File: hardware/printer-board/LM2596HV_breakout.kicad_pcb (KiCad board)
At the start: 2 copper layers, 50 x 30 mm, 13 parts, among them J1 VIN, J2 VOUT, U1 LM2596HVS

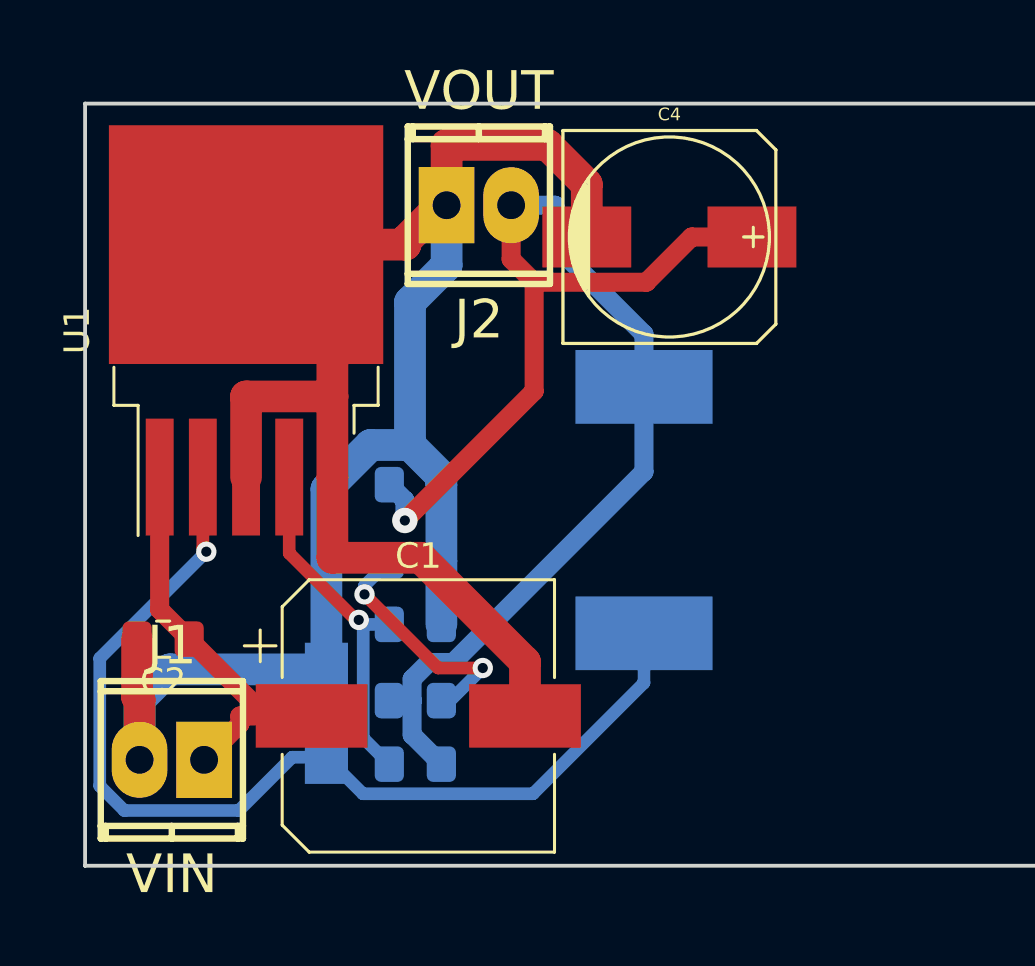
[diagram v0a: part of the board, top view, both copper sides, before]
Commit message: update power circuit,
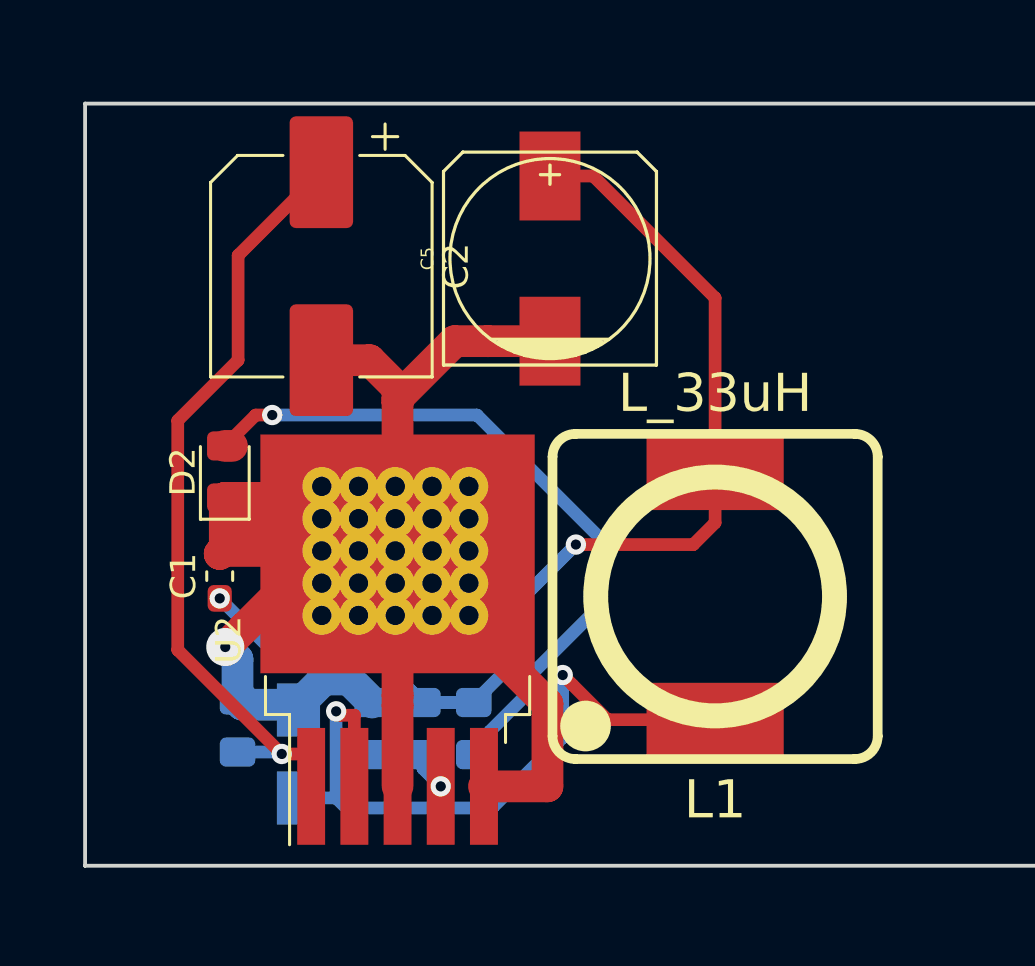
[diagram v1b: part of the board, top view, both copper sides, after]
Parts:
- removed C4: CP220uf,35V, w_smd_cap:c_elec_8x10.5
- removed J1: VIN, footprint-lib:mpt_0,5%2f2-2,54
- removed J2: VOUT, footprint-lib:mpt_0,5%2f2-2,54
- removed U1: LM2596HVS, Package_TO_SOT_SMD:TO-263-5_TabPin3
- added C5: CP220uf,35V, w_smd_cap:c_elec_8x10.5, F.Cu at (33.3, 21.1)
- added U2: LM2596HVS, footprint-lib:TO-263-5_TabPin3,heat_drill, F.Cu at (27.3, 36.1)
- C1: value CP100uf,63V -> C103,0603; footprint Capacitor_SMD:CP_Elec_10x10.5 -> Capacitor_SMD:C_0603_1608Metric_Pad1.05x0.95mm_HandSolder
- C2: value C103 -> CP100uf,50V; footprint Capacitor_SMD:C_0805_2012Metric_Pad1.15x1.40mm_HandSolder -> Capacitor_SMD:CP_Elec_8x10.5
- D2: value LED_GREEN -> 5V_STATUS; moved to F.Cu
- L1: moved to F.Cu
- R1: value RVAR -> R331
- R2: value R331 -> RVAR
- moved C2 15.9 mm to (24.3, 21.4), turned to 270 degrees
- moved C3 11.8 mm to (21.0, 39.5), turned to 90 degrees
- moved C1 9.56 mm to (20.3, 33.6), turned to 90 degrees
- moved D2 8.28 mm to (20.5, 29.5), turned to 90 degrees
- moved L1 4.40 mm to (39.8, 34.4), turned to 180 degrees
- moved R2 4.11 mm to (28.3, 39.6), turned to 270 degrees
- moved R3 2.55 mm to (30.3, 39.6), turned to 270 degrees
- moved R1 2.20 mm to (26.3, 39.6), turned to 270 degrees
- moved D1 1.94 mm to (23.4, 40.6)
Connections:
- C1 pad 1: VIN -> +5V
- C2 pad 1: VIN -> +12V
- C3 pad 1: VOUT -> +12V
- L1 pad 2: VOUT -> +5V
- R1 pad 1: VOUT -> GND
- R2 pad 1: GND -> +5V
- R3 pad 1: VOUT -> +5V
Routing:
- net VOUT: track 56.8 -> 0.00 mm, vias 1 -> 0
- net +5V: track 0.00 -> 42.8 mm, vias 0 -> 2
- net +12V: track 0.00 -> 31.1 mm, vias 0 -> 1
- net Net-(D2-Pad2): track 9.74 -> 28.1 mm, vias 2 -> 1
- net VIN: track 16.3 -> 0.00 mm
- net Net-(D1-Pad1): track 41.0 -> 27.9 mm, vias 1 -> 2
- net Net-(R1-Pad2): track 14.0 -> 3.54 mm
- net GND: track 93.7 -> 87.3 mm, vias 0 -> 1

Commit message: update for stepper Z,
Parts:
- added C10: CP100uf,25V, Capacitor_SMD:CP_Elec_6.3x7.7, F.Cu at (297.3, 53.2)
- added C11: C104,0603, Capacitor_SMD:C_0603_1608Metric_Pad1.05x0.95mm_HandSolder, F.Cu at (297.6, 59.1)
- added C12: CP100uf,25V, Capacitor_SMD:CP_Elec_6.3x7.7, F.Cu at (240.3, 109.1)
- added C13: C104,0603, Capacitor_SMD:C_0603_1608Metric_Pad1.05x0.95mm_HandSolder, F.Cu at (237.3, 115.0)
- added C14: C106,0603, Capacitor_SMD:C_0603_1608Metric_Pad1.05x0.95mm_HandSolder, F.Cu at (295.6, 127.7)
- added C15: C106,0603, Capacitor_SMD:C_0603_1608Metric_Pad1.05x0.95mm_HandSolder, F.Cu at (292.3, 136.8)
- added C16: C106,0603, Capacitor_SMD:C_0603_1608Metric_Pad1.05x0.95mm_HandSolder, F.Cu at (292.3, 127.7)
- added C17: C106,0603, Capacitor_SMD:C_0603_1608Metric_Pad1.05x0.95mm_HandSolder, F.Cu at (295.6, 129.2)
- added C18: C106,0603, Capacitor_SMD:C_0603_1608Metric_Pad1.05x0.95mm_HandSolder, F.Cu at (292.3, 132.3)
- added C19: C104,0603, Capacitor_SMD:C_0603_1608Metric_Pad1.05x0.95mm_HandSolder, F.Cu at (221.4, 140.3)
- added C20: CP100uf,35V, Capacitor_SMD:CP_Elec_6.3x7.7, F.Cu at (235.1, 137.6)
- added C21: C104,0603, Capacitor_SMD:C_0603_1608Metric_Pad1.05x0.95mm_HandSolder, F.Cu at (295.3, 86.0)
- added C22: C10pf,0603, Capacitor_SMD:C_0603_1608Metric_Pad1.05x0.95mm_HandSolder, F.Cu at (281.9, 85.8)
- added C23: C104,0603, Capacitor_SMD:C_0603_1608Metric_Pad1.05x0.95mm_HandSolder, F.Cu at (308.3, 76.8)
- added C24: C10pf,0603, Capacitor_SMD:C_0603_1608Metric_Pad1.05x0.95mm_HandSolder, F.Cu at (285.2, 85.8)
- added C25: C104,0603, Capacitor_SMD:C_0603_1608Metric_Pad1.05x0.95mm_HandSolder, F.Cu at (295.1, 82.0)
- added C26: C104,0603, Capacitor_SMD:C_0603_1608Metric_Pad1.05x0.95mm_HandSolder, F.Cu at (295.1, 80.4)
- added C27: C104,0603, Capacitor_SMD:C_0603_1608Metric_Pad1.05x0.95mm_HandSolder, F.Cu at (298.5, 80.4)
- added C28: C104,0603, Capacitor_SMD:C_0603_1608Metric_Pad1.05x0.95mm_HandSolder, F.Cu at (295.1, 83.5)
- added C29: C105,0603, Capacitor_SMD:C_0603_1608Metric_Pad1.05x0.95mm_HandSolder, F.Cu at (305.0, 75.3)
- added C30: C104,0603, Capacitor_SMD:C_0603_1608Metric_Pad1.05x0.95mm_HandSolder, F.Cu at (298.5, 78.9)
- added C31: C104,0603, Capacitor_SMD:C_0603_1608Metric_Pad1.05x0.95mm_HandSolder, F.Cu at (291.9, 85.8)
- added C32: C104,0603, Capacitor_SMD:C_0603_1608Metric_Pad1.05x0.95mm_HandSolder, F.Cu at (288.6, 85.8)
- added C33: CP220uf,16V, Capacitor_SMD:C_0603_1608Metric_Pad1.05x0.95mm_HandSolder, F.Cu at (147.7, 149.0)
- added C34: CP220uf,16V, Capacitor_SMD:C_0603_1608Metric_Pad1.05x0.95mm_HandSolder, F.Cu at (144.3, 149.0)
- added C35: CP220uf,25V, Capacitor_SMD:C_0603_1608Metric_Pad1.05x0.95mm_HandSolder, F.Cu at (144.3, 150.5)
- added C36: CP100uf,16V, Capacitor_SMD:CP_Elec_6.3x5.3, F.Cu at (259.2, 130.5)
- added C37: CP100uf,16V, Capacitor_SMD:CP_Elec_6.3x5.3, F.Cu at (321.8, 48.1)
- added C38: CP100uf,16V, Capacitor_SMD:CP_Elec_6.3x5.3, F.Cu at (259.2, 145.1)
- added C39: CP100uf,25V, Capacitor_SMD:CP_Elec_6.3x7.7, F.Cu at (257.2, 77.0)
- added C4: CP100uf,25V, Capacitor_SMD:CP_Elec_6.3x7.7, F.Cu at (200.2, 109.1)
- added C40: C104,0603, Capacitor_SMD:C_0603_1608Metric_Pad1.05x0.95mm_HandSolder, F.Cu at (254.2, 84.5)
- added C41: CP100uf,25V, Capacitor_SMD:CP_Elec_6.3x7.7, F.Cu at (257.2, 53.2)
- added C42: C104,0603, Capacitor_SMD:C_0603_1608Metric_Pad1.05x0.95mm_HandSolder, F.Cu at (263.6, 54.0)
- added C43: C104,0603, Capacitor_SMD:C_0603_1608Metric_Pad1.05x0.95mm_HandSolder, F.Cu at (274.0, 103.0)
- added C44: CP100uf,16V, Capacitor_SMD:CP_Elec_6.3x5.3, F.Cu at (280.3, 95.8)
- added C45: C106,0603, Capacitor_SMD:C_0603_1608Metric_Pad1.05x0.95mm_HandSolder, F.Cu at (318.6, 92.3)
- added C46: C104,0603, Capacitor_SMD:C_0603_1608Metric_Pad1.05x0.95mm_HandSolder, F.Cu at (325.3, 92.3)
- added C47: C332,0603, Capacitor_SMD:C_0603_1608Metric_Pad1.05x0.95mm_HandSolder, F.Cu at (322.0, 92.3)
- added C48: C103,0603, Capacitor_SMD:C_0603_1608Metric_Pad1.05x0.95mm_HandSolder, F.Cu at (318.6, 93.8)
- added C49: C226,6.3v,0603, Capacitor_SMD:C_0603_1608Metric_Pad1.05x0.95mm_HandSolder, F.Cu at (328.7, 93.8)
- added C50: C106,0603, Capacitor_SMD:C_0603_1608Metric_Pad1.05x0.95mm_HandSolder, F.Cu at (224.8, 152.9)
- added C51: C104,0603, Capacitor_SMD:C_0603_1608Metric_Pad1.05x0.95mm_HandSolder, F.Cu at (228.1, 151.4)
- added C52: C332,0603, Capacitor_SMD:C_0603_1608Metric_Pad1.05x0.95mm_HandSolder, F.Cu at (221.4, 152.9)
- added C53: C103,0603, Capacitor_SMD:C_0603_1608Metric_Pad1.05x0.95mm_HandSolder, F.Cu at (224.8, 151.4)
- added C54: C226,6.3v,0603, Capacitor_SMD:C_0603_1608Metric_Pad1.05x0.95mm_HandSolder, F.Cu at (221.4, 151.4)
- added C6: CP100uf,25V, Capacitor_SMD:CP_Elec_6.3x7.7, F.Cu at (160.0, 133.1)
- added C7: C104,0603, Capacitor_SMD:C_0603_1608Metric_Pad1.05x0.95mm_HandSolder, F.Cu at (160.3, 139.0)
- added C8: CP100uf,25V, Capacitor_SMD:CP_Elec_6.3x7.7, F.Cu at (200.1, 133.1)
- added C9: C104,0603, Capacitor_SMD:C_0603_1608Metric_Pad1.05x0.95mm_HandSolder, F.Cu at (197.1, 140.5)
- added D10: LED_BLUE,0603, LED_SMD:LED_0603_1608Metric_Pad1.05x0.95mm_HandSolder, F.Cu at (315.2, 79.3)
- added D11: LED_BLUE,0603, LED_SMD:LED_0603_1608Metric_Pad1.05x0.95mm_HandSolder, F.Cu at (318.6, 79.3)
- added D12: LED_BLUE,0603, LED_SMD:LED_0603_1608Metric_Pad1.05x0.95mm_HandSolder, F.Cu at (318.6, 80.9)
- added D13: LED_BLUE,0603, LED_SMD:LED_0603_1608Metric_Pad1.05x0.95mm_HandSolder, F.Cu at (325.4, 79.3)
- added D14: LED_BLUE,0603, LED_SMD:LED_0603_1608Metric_Pad1.05x0.95mm_HandSolder, F.Cu at (322.0, 79.3)
- added D15: SD_M4, Diode_SMD:D_SOD-323_HandSoldering, F.Cu at (221.8, 136.1)
- added D16: SD_M4, Diode_SMD:D_SOD-323_HandSoldering, F.Cu at (225.8, 136.1)
- added D17: PB9, LED_SMD:LED_0603_1608Metric_Pad1.05x0.95mm_HandSolder, F.Cu at (278.5, 85.8)
- added D18: LED_RED,0603, LED_SMD:LED_0603_1608Metric_Pad1.05x0.95mm_HandSolder, F.Cu at (295.3, 102.5)
- added D19: LED_RED,0603, LED_SMD:LED_0603_1608Metric_Pad1.05x0.95mm_HandSolder, F.Cu at (265.4, 122.5)
- added D20: LED_BLUE,0603, LED_SMD:LED_0603_1608Metric_Pad1.05x0.95mm_HandSolder, F.Cu at (259.8, 134.9)
- added D21: LED_BLUE,0603, LED_SMD:LED_0603_1608Metric_Pad1.05x0.95mm_HandSolder, F.Cu at (322.4, 52.4)
- added D22: LED_BLUE,0603, LED_SMD:LED_0603_1608Metric_Pad1.05x0.95mm_HandSolder, F.Cu at (272.1, 142.3)
- added D23: LED_BLUE,0603, LED_SMD:LED_0603_1608Metric_Pad1.05x0.95mm_HandSolder, F.Cu at (254.2, 81.4)
- added D24: LED_BLUE,0603, LED_SMD:LED_0603_1608Metric_Pad1.05x0.95mm_HandSolder, F.Cu at (254.2, 57.5)
- added D3: LED_BLUE,0603, LED_SMD:LED_0603_1608Metric_Pad1.05x0.95mm_HandSolder, F.Cu at (197.2, 113.5)
- added D4: LED_BLUE,0603, LED_SMD:LED_0603_1608Metric_Pad1.05x0.95mm_HandSolder, F.Cu at (157.0, 137.4)
- added D5: LED_BLUE,0603, LED_SMD:LED_0603_1608Metric_Pad1.05x0.95mm_HandSolder, F.Cu at (197.1, 137.4)
- added D6: LED_BLUE,0603, LED_SMD:LED_0603_1608Metric_Pad1.05x0.95mm_HandSolder, F.Cu at (294.3, 57.5)
- added D7: LED_BLUE,0603, LED_SMD:LED_0603_1608Metric_Pad1.05x0.95mm_HandSolder, F.Cu at (237.3, 113.5)
- added D8: LED_RED,0603, LED_SMD:LED_0603_1608Metric_Pad1.05x0.95mm_HandSolder, F.Cu at (295.3, 119.1)
- added D9: LED_BLUE,0603, LED_SMD:LED_0603_1608Metric_Pad1.05x0.95mm_HandSolder, F.Cu at (315.2, 80.9)
- added F1: 16V/30A, w_misc_comp:fuse_smf, F.Cu at (225.0, 127.0)
- added F2: 30V/5A, w_misc_comp:fuse_smf, F.Cu at (225.0, 132.4)
- added H1: MOUNT_M3, MountingHole:MountingHole_2.7mm_M2.5, F.Cu at (3.00, 3.00)
- added H2: MOUNT_M3, MountingHole:MountingHole_2.7mm_M2.5, F.Cu at (97.0, 3.00)
- added H3: MOUNT_M3, MountingHole:MountingHole_2.7mm_M2.5, F.Cu at (3.00, 97.0)
- added H4: MOUNT_M3, MountingHole:MountingHole_2.7mm_M2.5, F.Cu at (97.0, 97.0)
- added J1: USB_DEBUG, Connector_PinHeader_1.27mm:PinHeader_1x05_P1.27mm_Vertical, F.Cu at (187.4, 45.7)
- added J10: MS_SELECT, Connector_PinHeader_2.54mm:PinHeader_2x03_P2.54mm_Vertical, F.Cu at (304.8, 46.3)
- added J11: E0, footprint-lib:b4b-ph-kl,stepper_terminal, F.Cu at (297.8, 46.6)
- added J12: MS_SELECT, Connector_PinHeader_2.54mm:PinHeader_2x03_P2.54mm_Vertical, F.Cu at (247.8, 102.3)
- added J13: E1, footprint-lib:b4b-ph-kl,stepper_terminal, F.Cu at (240.8, 102.6)
- added J14: HEATBED, footprint-lib:mpt_0,5%2f2-2,54,heatbed, F.Cu at (309.5, 113.4)
- added J15: X_MIN, footprint-lib:b3b-ph-kl,end_stop, F.Cu at (317.7, 70.5)
- added J16: X_MAX, footprint-lib:b3b-ph-kl,end_stop, F.Cu at (317.7, 75.6)
- added J17: Y_MIN, footprint-lib:b3b-ph-kl,end_stop, F.Cu at (326.1, 70.5)
- added J18: Y_MAX, footprint-lib:b3b-ph-kl,end_stop, F.Cu at (326.1, 75.6)
- added J19: Z_MIN, footprint-lib:b3b-ph-kl,end_stop, F.Cu at (334.5, 70.5)
- added J2: MS_SELECT, Connector_PinHeader_2.54mm:PinHeader_2x03_P2.54mm_Vertical, F.Cu at (167.5, 102.3)
- added J20: Z_MAX, footprint-lib:b3b-ph-kl,end_stop, F.Cu at (334.5, 75.6)
- added J21: HEATBED_TEMP, w_conn_jst-ph:b2b-ph-kl, F.Cu at (281.1, 134.1)
- added J22: HOTEND_TEMP0, w_conn_jst-ph:b2b-ph-kl, F.Cu at (281.1, 129.1)
- added J23: HOTEND_TEMP1, w_conn_jst-ph:b2b-ph-kl, F.Cu at (287.4, 129.1)
- added J24: AUX_TEMP, w_conn_jst-ph:b2b-ph-kl, F.Cu at (287.4, 134.1)
- added J25: 12V_INPUT_2, footprint-lib:mpt_0,5%2f2-2,54,12V_SRC, F.Cu at (245.3, 130.8)
- added J26: 12V_INPUT, footprint-lib:mpt_0,5%2f2-2,54,12V_SRC, F.Cu at (239.3, 130.8)
- added J27: 12V_OUT, footprint-lib:mpt_0,5%2f2-2,54,12V_SRC, F.Cu at (233.3, 130.8)
- added J28: SWD, Connector_PinHeader_1.27mm:PinHeader_1x04_P1.27mm_Vertical, F.Cu at (307.2, 69.6)
- added J29: USB_DEBUG, Connector_PinHeader_1.27mm:PinHeader_1x05_P1.27mm_Vertical, F.Cu at (157.4, 149.5)
- added J3: X, footprint-lib:b4b-ph-kl,stepper_terminal, F.Cu at (160.5, 102.6)
- added J30: PWR_DEBUG, Connector_PinHeader_1.27mm:PinHeader_1x05_P1.27mm_Vertical, F.Cu at (141.1, 149.5)
- added J31: HOT_END, footprint-lib:mpt_0,5%2f2-2,54,heatbed, F.Cu at (309.5, 96.8)
- added J32: HOT_END, footprint-lib:mpt_0,5%2f2-2,54,heatbed, F.Cu at (279.6, 116.8)
- added J33: TO FAN0, footprint-lib:b2b-ph-kl,fan_pwm_out, F.Cu at (267.2, 129.1)
- added J34: TO FAN1, footprint-lib:b2b-ph-kl,fan_pwm_out, F.Cu at (329.8, 46.6)
- added J35: TO FAN2, footprint-lib:b2b-ph-kl,fan_pwm_out, F.Cu at (267.2, 143.6)
- added J36: MS_SELECT, Connector_PinHeader_2.54mm:PinHeader_2x03_P2.54mm_Vertical, F.Cu at (264.7, 70.2)
- added J37: Z2, footprint-lib:b4b-ph-kl,stepper_terminal, F.Cu at (257.7, 70.5)
- added J38: MS_SELECT, Connector_PinHeader_2.54mm:PinHeader_2x03_P2.54mm_Vertical, F.Cu at (264.7, 46.3)
- added J39: Y, footprint-lib:b4b-ph-kl,stepper_terminal, F.Cu at (257.7, 46.6)
- added J4: MS_SELECT, Connector_PinHeader_2.54mm:PinHeader_2x03_P2.54mm_Vertical, F.Cu at (207.7, 102.3)
- added J40: Conn_01x07, Connector_PinHeader_1.27mm:PinHeader_1x07_P1.27mm_Vertical, F.Cu at (273.9, 93.4)
- added J41: EXP1, Connector_PinHeader_2.54mm:PinHeader_2x05_P2.54mm_Vertical, F.Cu at (261.8, 94.1)
- added J42: EXP2, Connector_PinHeader_2.54mm:PinHeader_2x05_P2.54mm_Vertical, F.Cu at (268.0, 94.1)
- added J5: Z, footprint-lib:b4b-ph-kl,stepper_terminal, F.Cu at (200.7, 102.6)
- added J6: MS_SELECT, Connector_PinHeader_2.54mm:PinHeader_2x03_P2.54mm_Vertical, F.Cu at (167.5, 126.2)
- added J7: Z1, footprint-lib:b4b-ph-kl,stepper_terminal, F.Cu at (160.5, 126.5)
- added J8: MS_SELECT, Connector_PinHeader_2.54mm:PinHeader_2x03_P2.54mm_Vertical, F.Cu at (207.6, 126.2)
- added J9: Z3, footprint-lib:b4b-ph-kl,stepper_terminal, F.Cu at (200.6, 126.5)
- added JP1: Jumper_NO_Small, Jumper:SolderJumper-2_P1.3mm_Open_TrianglePad1.0x1.5mm, F.Cu at (141.2, 95.7)
- added JP2: Jumper_NO_Small, Jumper:SolderJumper-2_P1.3mm_Open_TrianglePad1.0x1.5mm, F.Cu at (187.5, 54.7)
- added JP3: Jumper_NO_Small, Jumper:SolderJumper-2_P1.3mm_Open_TrianglePad1.0x1.5mm, F.Cu at (194.0, 45.8)
- added JP4: Jumper_NO_Small, Jumper:SolderJumper-2_P1.3mm_Open_TrianglePad1.0x1.5mm, F.Cu at (144.6, 94.1)
- added JP5: Jumper_NO_Small, SolderJumper-2_P1.3mm_Open_TrianglePad1.0x1.5mm, F.Cu at (221.4, 138.3)
- added JP6: Jumper_NO_Small, SolderJumper-2_P1.3mm_Open_TrianglePad1.0x1.5mm, F.Cu at (298.5, 84.0)
- added JP7: Jumper_NO_Small, SolderJumper-2_P1.3mm_Open_TrianglePad1.0x1.5mm, F.Cu at (305.2, 78.8)
- added L2: L_15uH, w_smd_inductors:inductor_smd_4.8x2.8mm, F.Cu at (327.2, 88.8)
- added L3: L_15uH, w_smd_inductors:inductor_smd_4.8x2.8mm, F.Cu at (229.9, 147.9)
- added Q1: WSK220N04, footprint-lib:TO-263-2,drill_array, F.Cu at (298.1, 112.6)
- added Q2: STP55NF06, footprint-lib:TO-263-2,drill_array, F.Cu at (298.1, 96.0)
- added Q3: STP55NF06, footprint-lib:TO-263-2,drill_array, F.Cu at (268.3, 116.0)
- added Q4: D882, footprint-lib:SOT-89-3,thermal_vias, F.Cu at (266.5, 134.6)
- added Q5: D882, footprint-lib:SOT-89-3,thermal_vias, F.Cu at (329.1, 52.2)
- added Q6: D882, footprint-lib:SOT-89-3,thermal_vias, F.Cu at (266.5, 149.2)
- added R10: R103,0603, Resistor_SMD:R_0603_1608Metric_Pad1.05x0.95mm_HandSolder, F.Cu at (160.4, 115.4)
- added R11: R104,0603, Resistor_SMD:R_0603_1608Metric_Pad1.05x0.95mm_HandSolder, F.Cu at (197.2, 115.0)
- added R12: R102,0603, Resistor_SMD:R_0603_1608Metric_Pad1.05x0.95mm_HandSolder, F.Cu at (206.6, 109.9)
- added R13: R103,0603, Resistor_SMD:R_0603_1608Metric_Pad1.05x0.95mm_HandSolder, F.Cu at (200.5, 115.0)
- added R14: R104,0603, Resistor_SMD:R_0603_1608Metric_Pad1.05x0.95mm_HandSolder, F.Cu at (166.4, 133.9)
- added R15: R102,0603, Resistor_SMD:R_0603_1608Metric_Pad1.05x0.95mm_HandSolder, F.Cu at (157.0, 139.0)
- added R16: R103,0603, Resistor_SMD:R_0603_1608Metric_Pad1.05x0.95mm_HandSolder, F.Cu at (157.0, 140.5)
- added R17: R104,0603, Resistor_SMD:R_0603_1608Metric_Pad1.05x0.95mm_HandSolder, F.Cu at (197.1, 139.0)
- added R18: R102,0603, Resistor_SMD:R_0603_1608Metric_Pad1.05x0.95mm_HandSolder, F.Cu at (206.5, 133.9)
- added R19: R103,0603, Resistor_SMD:R_0603_1608Metric_Pad1.05x0.95mm_HandSolder, F.Cu at (200.4, 139.0)
- added R20: R104,0603, Resistor_SMD:R_0603_1608Metric_Pad1.05x0.95mm_HandSolder, F.Cu at (303.7, 54.0)
- added R21: R102,0603, Resistor_SMD:R_0603_1608Metric_Pad1.05x0.95mm_HandSolder, F.Cu at (294.3, 60.6)
- added R22: R103,0603, Resistor_SMD:R_0603_1608Metric_Pad1.05x0.95mm_HandSolder, F.Cu at (294.3, 59.1)
- added R23: R104,0603, Resistor_SMD:R_0603_1608Metric_Pad1.05x0.95mm_HandSolder, F.Cu at (240.6, 115.0)
- added R24: R102,0603, Resistor_SMD:R_0603_1608Metric_Pad1.05x0.95mm_HandSolder, F.Cu at (246.7, 109.9)
- added R25: R103,0603, Resistor_SMD:R_0603_1608Metric_Pad1.05x0.95mm_HandSolder, F.Cu at (237.3, 116.6)
- added R26: R100,0805, Resistor_SMD:R_0805_2012Metric_Pad1.15x1.40mm_HandSolder, F.Cu at (308.3, 117.6)
- added R27: R104,0805, Resistor_SMD:R_0805_2012Metric_Pad1.15x1.40mm_HandSolder, F.Cu at (291.7, 119.3)
- added R28: R182,0603, Resistor_SMD:R_0603_1608Metric_Pad1.05x0.95mm_HandSolder, F.Cu at (298.6, 119.0)
- added R29: R102,0603, Resistor_SMD:R_0603_1608Metric_Pad1.05x0.95mm_HandSolder, F.Cu at (332.0, 82.3)
- added R30: R102,0603, Resistor_SMD:R_0603_1608Metric_Pad1.05x0.95mm_HandSolder, F.Cu at (328.7, 79.3)
- added R31: R102,0603, Resistor_SMD:R_0603_1608Metric_Pad1.05x0.95mm_HandSolder, F.Cu at (325.3, 80.9)
- added R32: R102,0603, Resistor_SMD:R_0603_1608Metric_Pad1.05x0.95mm_HandSolder, F.Cu at (328.7, 80.8)
- added R33: R102,0603, Resistor_SMD:R_0603_1608Metric_Pad1.05x0.95mm_HandSolder, F.Cu at (328.7, 82.3)
- added R34: R102,0603, Resistor_SMD:R_0603_1608Metric_Pad1.05x0.95mm_HandSolder, F.Cu at (322.0, 80.9)
- added R35: R472,0603, Resistor_SMD:R_0603_1608Metric_Pad1.05x0.95mm_HandSolder, F.Cu at (292.3, 129.2)
- added R36: R472,0603, Resistor_SMD:R_0603_1608Metric_Pad1.05x0.95mm_HandSolder, F.Cu at (292.3, 130.7)
- added R37: R472,0603, Resistor_SMD:R_0603_1608Metric_Pad1.05x0.95mm_HandSolder, F.Cu at (292.3, 135.3)
- added R38: R472,0603, Resistor_SMD:R_0603_1608Metric_Pad1.05x0.95mm_HandSolder, F.Cu at (295.6, 132.3)
- added R39: R472,0603, Resistor_SMD:R_0603_1608Metric_Pad1.05x0.95mm_HandSolder, F.Cu at (292.3, 133.8)
- added R4: R220,0603, Resistor_SMD:R_0603_1608Metric_Pad1.05x0.95mm_HandSolder, F.Cu at (187.5, 52.7)
- added R40: R472,0603, Resistor_SMD:R_0603_1608Metric_Pad1.05x0.95mm_HandSolder, F.Cu at (301.8, 82.0)
- added R41: R472,0603, Resistor_SMD:R_0603_1608Metric_Pad1.05x0.95mm_HandSolder, F.Cu at (301.8, 80.4)
- added R42: R0,0603, Resistor_SMD:R_0603_1608Metric_Pad1.05x0.95mm_HandSolder, F.Cu at (308.3, 75.3)
- added R43: R0,0603, Resistor_SMD:R_0603_1608Metric_Pad1.05x0.95mm_HandSolder, F.Cu at (295.1, 78.9)
- added R44: R102,0603, Resistor_SMD:R_0603_1608Metric_Pad1.05x0.95mm_HandSolder, F.Cu at (301.8, 78.9)
- added R45: R103,0603, Resistor_SMD:R_0603_1608Metric_Pad1.05x0.95mm_HandSolder, F.Cu at (305.0, 76.8)
- added R46: R103,0603, Resistor_SMD:R_0603_1608Metric_Pad1.05x0.95mm_HandSolder, F.Cu at (298.5, 82.0)
- added R47: R220,0603, Resistor_SMD:R_0603_1608Metric_Pad1.05x0.95mm_HandSolder, F.Cu at (160.7, 150.5)
- added R48: R220,0603, Resistor_SMD:R_0603_1608Metric_Pad1.05x0.95mm_HandSolder, F.Cu at (164.0, 149.0)
- added R49: R152,0603, Resistor_SMD:R_0603_1608Metric_Pad1.05x0.95mm_HandSolder, F.Cu at (160.7, 149.0)
- added R5: R220,0603, Resistor_SMD:R_0603_1608Metric_Pad1.05x0.95mm_HandSolder, F.Cu at (147.9, 93.6)
- added R50: R100,0805, Resistor_SMD:R_0805_2012Metric_Pad1.15x1.40mm_HandSolder, F.Cu at (308.3, 101.0)
- added R51: R104,0805, Resistor_SMD:R_0805_2012Metric_Pad1.15x1.40mm_HandSolder, F.Cu at (291.7, 102.7)
- added R52: R182,0603, Resistor_SMD:R_0603_1608Metric_Pad1.05x0.95mm_HandSolder, F.Cu at (298.6, 102.4)
- added R53: R100,0805, Resistor_SMD:R_0805_2012Metric_Pad1.15x1.40mm_HandSolder, F.Cu at (261.8, 122.7)
- added R54: R104,0805, Resistor_SMD:R_0805_2012Metric_Pad1.15x1.40mm_HandSolder, F.Cu at (278.5, 121.0)
- added R55: R182,0603, Resistor_SMD:R_0603_1608Metric_Pad1.05x0.95mm_HandSolder, F.Cu at (268.8, 122.5)
- added R56: R100,0805, Resistor_SMD:R_0805_2012Metric_Pad1.15x1.40mm_HandSolder, F.Cu at (272.3, 127.9)
- added R57: R104,0805, Resistor_SMD:R_0805_2012Metric_Pad1.15x1.40mm_HandSolder, F.Cu at (256.2, 135.1)
- added R58: R100,0603, Resistor_SMD:R_0603_1608Metric_Pad1.05x0.95mm_HandSolder, F.Cu at (259.4, 136.8)
- added R59: R182,0603, Resistor_SMD:R_0603_1608Metric_Pad1.05x0.95mm_HandSolder, F.Cu at (256.0, 136.8)
- added R6: R152,0603, Resistor_SMD:R_0603_1608Metric_Pad1.05x0.95mm_HandSolder, F.Cu at (190.6, 48.3)
- added R60: R100,0805, Resistor_SMD:R_0805_2012Metric_Pad1.15x1.40mm_HandSolder, F.Cu at (334.8, 45.5)
- added R61: R104,0805, Resistor_SMD:R_0805_2012Metric_Pad1.15x1.40mm_HandSolder, F.Cu at (318.8, 52.6)
- added R62: R100,0603, Resistor_SMD:R_0603_1608Metric_Pad1.05x0.95mm_HandSolder, F.Cu at (318.6, 54.4)
- added R63: R182,0603, Resistor_SMD:R_0603_1608Metric_Pad1.05x0.95mm_HandSolder, F.Cu at (322.0, 54.4)
- added R64: R100,0805, Resistor_SMD:R_0603_1608Metric_Pad1.05x0.95mm_HandSolder, F.Cu at (259.8, 149.4)
- added R65: R104,0805, Resistor_SMD:R_0805_2012Metric_Pad1.15x1.40mm_HandSolder, F.Cu at (256.2, 149.6)
- added R66: R100,0603, Resistor_SMD:R_0603_1608Metric_Pad1.05x0.95mm_HandSolder, F.Cu at (256.0, 151.4)
- added R67: R182,0603, Resistor_SMD:R_0603_1608Metric_Pad1.05x0.95mm_HandSolder, F.Cu at (259.4, 151.4)
- added R68: R104,0603, Resistor_SMD:R_0603_1608Metric_Pad1.05x0.95mm_HandSolder, F.Cu at (257.5, 83.0)
- added R69: R102,0603, Resistor_SMD:R_0603_1608Metric_Pad1.05x0.95mm_HandSolder, F.Cu at (254.2, 83.0)
- added R7: R102,0603, Resistor_SMD:R_0603_1608Metric_Pad1.05x0.95mm_HandSolder, F.Cu at (190.6, 46.8)
- added R70: R103,0603, Resistor_SMD:R_0603_1608Metric_Pad1.05x0.95mm_HandSolder, F.Cu at (263.6, 77.8)
- added R71: R104,0603, Resistor_SMD:R_0603_1608Metric_Pad1.05x0.95mm_HandSolder, F.Cu at (257.5, 59.1)
- added R72: R102,0603, Resistor_SMD:R_0603_1608Metric_Pad1.05x0.95mm_HandSolder, F.Cu at (254.2, 60.6)
- added R73: R103,0603, Resistor_SMD:R_0603_1608Metric_Pad1.05x0.95mm_HandSolder, F.Cu at (254.2, 59.1)
- added R74: R562,0603, Resistor_SMD:R_0603_1608Metric_Pad1.05x0.95mm_HandSolder, F.Cu at (328.7, 92.3)
- added R75: R103,0603, Resistor_SMD:R_0603_1608Metric_Pad1.05x0.95mm_HandSolder, F.Cu at (325.3, 93.8)
- added R76: R333,0603, Resistor_SMD:R_0603_1608Metric_Pad1.05x0.95mm_HandSolder, F.Cu at (322.0, 93.8)
- added R77: R562,0603, Resistor_SMD:R_0603_1608Metric_Pad1.05x0.95mm_HandSolder, F.Cu at (228.1, 152.9)
- added R78: R103,0603, Resistor_SMD:R_0603_1608Metric_Pad1.05x0.95mm_HandSolder, F.Cu at (231.5, 151.4)
- added R79: R333,0603, Resistor_SMD:R_0603_1608Metric_Pad1.05x0.95mm_HandSolder, F.Cu at (231.5, 152.9)
- added R8: R104,0603, Resistor_SMD:R_0805_2012Metric_Pad1.15x1.40mm_HandSolder, F.Cu at (157.2, 113.7)
- added R9: R102,0603, Resistor_SMD:R_0603_1608Metric_Pad1.05x0.95mm_HandSolder, F.Cu at (157.0, 117.0)
- added SW1: SW_Push, Button_Switch_SMD:SW_SPST_CK_RS282G05A3, F.Cu at (298.4, 76.1)
- added TH1: Thermistor_NTC, Resistor_SMD:R_0603_1608Metric_Pad1.05x0.95mm_HandSolder, F.Cu at (295.6, 130.7)
- added U1: orange_pi_zero, footprint-lib:orangepi-zero, F.Cu at (139.8, 92.6)
- added U10: A4988_MODULE, footprint-lib:Pololu_Breakout-16_15.2x20.3mm, F.Cu at (238.2, 46.0)
- added U11: MP2303A_ALT, footprint-lib:SOIC-8_3.9x4.9mm_P1.27mm,thermal_via, F.Cu at (320.7, 88.8)
- added U12: MP2303A_ALT, footprint-lib:SOIC-8_3.9x4.9mm_P1.27mm,thermal_via, F.Cu at (223.5, 147.9)
- added U3: A4988_MODULE, footprint-lib:Pololu_Breakout-16_15.2x20.3mm, F.Cu at (181.3, 102.0)
- added U4: A4988_MODULE, footprint-lib:Pololu_Breakout-16_15.2x20.3mm, F.Cu at (141.1, 125.9)
- added U5: A4988_MODULE, footprint-lib:Pololu_Breakout-16_15.2x20.3mm, F.Cu at (181.2, 125.9)
- added U6: A4988_MODULE, footprint-lib:Pololu_Breakout-16_15.2x20.3mm, F.Cu at (278.4, 46.0)
- added U7: A4988_MODULE, footprint-lib:Pololu_Breakout-16_15.2x20.3mm, F.Cu at (221.4, 102.0)
- added U8: STM32F407VET6, w_smd_lqfp:TQFP-100, F.Cu at (285.1, 76.7)
- added U9: A4988_MODULE, footprint-lib:Pololu_Breakout-16_15.2x20.3mm, F.Cu at (238.2, 69.9)
- added Y1: O_8M, Crystal:Crystal_HC49-4H_Vertical, F.Cu at (297.1, 71.2)
- C1: value C103,0603 -> CP100uf,35V
- C2: value CP100uf,50V -> CP100uf,25V; footprint Capacitor_SMD:CP_Elec_8x10.5 -> Capacitor_SMD:CP_Elec_6.3x7.7
- C3: value C103 -> C104,0603; footprint Capacitor_SMD:C_0805_2012Metric_Pad1.15x1.40mm_HandSolder -> Capacitor_SMD:C_0603_1608Metric_Pad1.05x0.95mm_HandSolder; moved to F.Cu
- C5: value CP220uf,35V -> C104,0603; footprint w_smd_cap:c_elec_8x10.5 -> Capacitor_SMD:C_0603_1608Metric_Pad1.05x0.95mm_HandSolder
- D1: value 1N5824 -> 5V HEALTHY; footprint w_smd_diode:do214ac -> LED_SMD:LED_0603_1608Metric_Pad1.05x0.95mm_HandSolder; moved to F.Cu
- D2: value 5V_STATUS -> LED_BLUE,0603; footprint LED_SMD:LED_0805_2012Metric_Pad1.15x1.40mm_HandSolder -> LED_SMD:LED_0603_1608Metric_Pad1.05x0.95mm_HandSolder
- L1: value L_33uH -> L_Small; footprint w_smd_inductors:inductor_smd_12.5x7.5mm -> w_smd_inductors:inductor_smd_0603
- R1: value R331 -> R153,0603; footprint Resistor_SMD:R_0805_2012Metric_Pad1.15x1.40mm_HandSolder -> Resistor_SMD:R_0603_1608Metric_Pad1.05x0.95mm_HandSolder; moved to F.Cu
- R2: value RVAR -> R153,0603; footprint Resistor_SMD:R_0805_2012Metric_Pad1.15x1.40mm_HandSolder -> Resistor_SMD:R_0603_1608Metric_Pad1.05x0.95mm_HandSolder; moved to F.Cu
- R3: value R511 -> R152,0603; footprint Resistor_SMD:R_0805_2012Metric_Pad1.15x1.40mm_HandSolder -> Resistor_SMD:R_0603_1608Metric_Pad1.05x0.95mm_HandSolder; moved to F.Cu
- U2: value LM2596HVS -> A4988_MODULE; footprint footprint-lib:TO-263-5_TabPin3,heat_drill -> footprint-lib:Pololu_Breakout-16_15.2x20.3mm
- moved L1 266.1 mm to (301.3, 83.4), turned to 0 degrees
- moved R1 219.1 mm to (238.4, 94.5), turned to 0 degrees
- moved R3 218.1 mm to (241.7, 93.0), turned to 0 degrees
- moved R2 216.7 mm to (238.4, 93.0), turned to 0 degrees
- moved C5 189.6 mm to (197.2, 116.6), turned to 0 degrees
- moved C1 170.7 mm to (190.6, 45.3), turned to 0 degrees
- moved C2 161.6 mm to (160.0, 109.1), turned to 0 degrees
- moved C3 161.6 mm to (166.4, 109.9), turned to 0 degrees
- moved D2 161.3 mm to (157.0, 115.4), turned to 0 degrees
- moved U2 131.5 mm to (141.1, 102.0), turned to 0 degrees
- moved D1 129.2 mm to (141.2, 93.6), turned to 0 degrees
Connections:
- C1 pad 1: +5V -> +3V3
- C3 pad 1: +12V -> GND
- C3 pad 2: GND -> +3V3
- C5 pad 1: +5V -> GND
- C5 pad 2: GND -> +3V3
- D1 pad 1: Net-(D1-Pad1) -> GND
- D1 pad 2: GND -> Net-(D1-Pad2)
- D2 pad 1: GND -> /X_~E1_STEP~PER_DRIVER/~X_EN~
- L1 pad 1: Net-(D1-Pad1) -> +3V3
- L1 pad 2: +5V -> Net-(C21-Pad1)
- R1 pad 1: GND -> /orange_pi/OPI_USB-DP2
- R1 pad 2: Net-(R1-Pad2) -> GND
- R2 pad 1: +5V -> /orange_pi/OPI_USB-DM2
- R2 pad 2: Net-(R1-Pad2) -> GND
- R3 pad 1: +5V -> +3V3
- R3 pad 2: Net-(D2-Pad2) -> /orange_pi/OPI_USB-DP2
- U2 pad 1: +12V -> /X_~E1_STEP~PER_DRIVER/~X_EN~
- U2 pad 2: Net-(D1-Pad1) -> Net-(J2-Pad1)
- U2 pad 3: GND -> Net-(J2-Pad3)
- U2 pad 4: Net-(R1-Pad2) -> Net-(J2-Pad5)
- U2 pad 5: GND -> Net-(U2-Pad5)
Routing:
- net GND: track 87.3 -> 0.00 mm, vias 1 -> 0
- net +5V: track 42.8 -> 0.00 mm, vias 2 -> 0
- net +12V: track 31.1 -> 0.00 mm, vias 1 -> 0
- net Net-(D2-Pad2): track 28.1 -> 0.00 mm, vias 1 -> 0
- net Net-(D1-Pad1): track 27.9 -> 0.00 mm, vias 2 -> 0
- net Net-(R1-Pad2): track 3.54 -> 0.00 mm, vias 1 -> 0
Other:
- board size 50 x 30 mm -> 100 x 100 mm
- net class Default: trace_width 0.5 -> 0.25
- net class GND removed
- net class PWR removed
- rule pad_to_mask_clearance: 0.051 -> 0
